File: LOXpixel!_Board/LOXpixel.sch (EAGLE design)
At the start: 18 parts, among them IC2 7805T, Q1 BSS138, Q2 BSS138

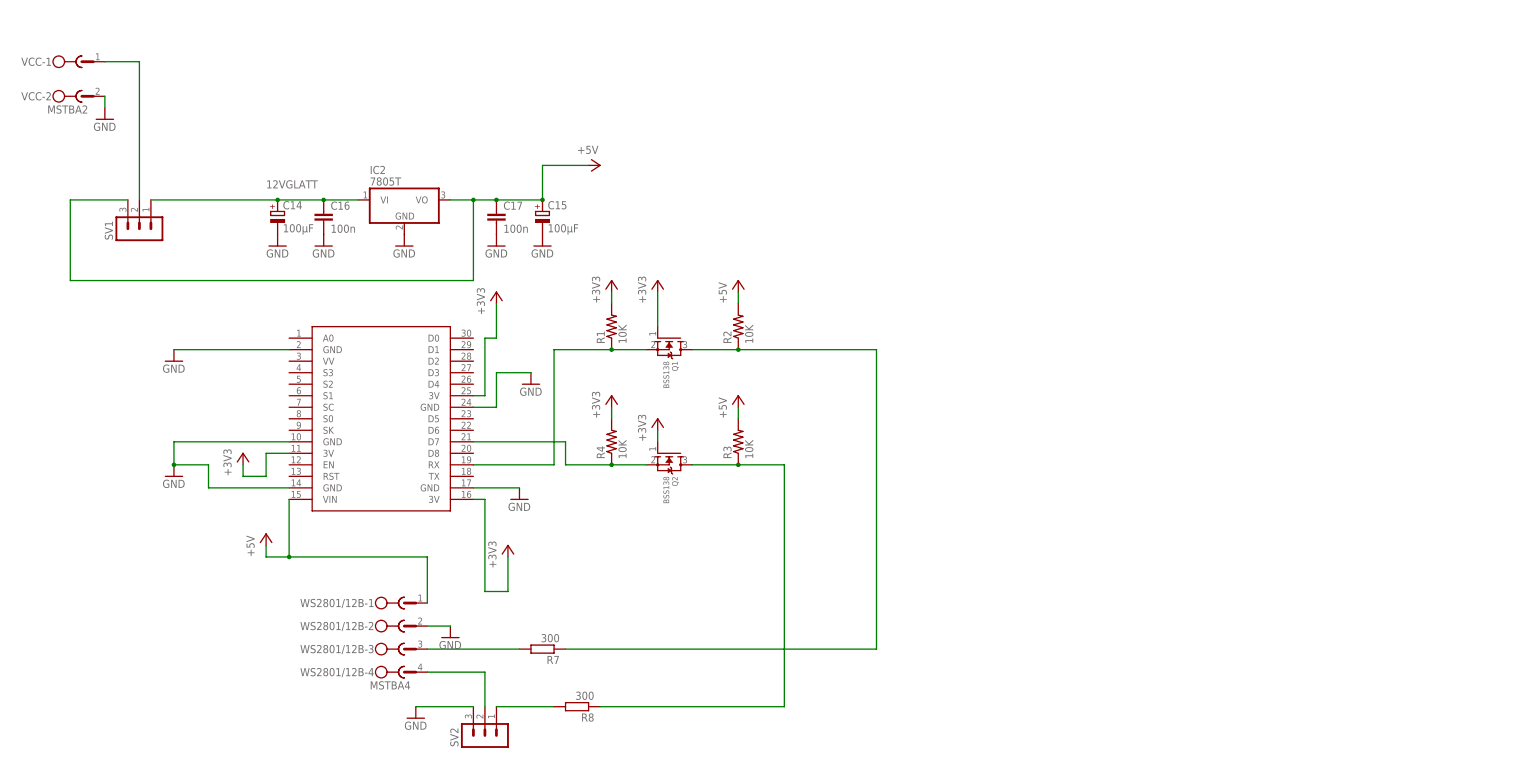
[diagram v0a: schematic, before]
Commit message: pcb for hammond 1551usb3 and rebuild without nodemcu and for esp-wroom-02
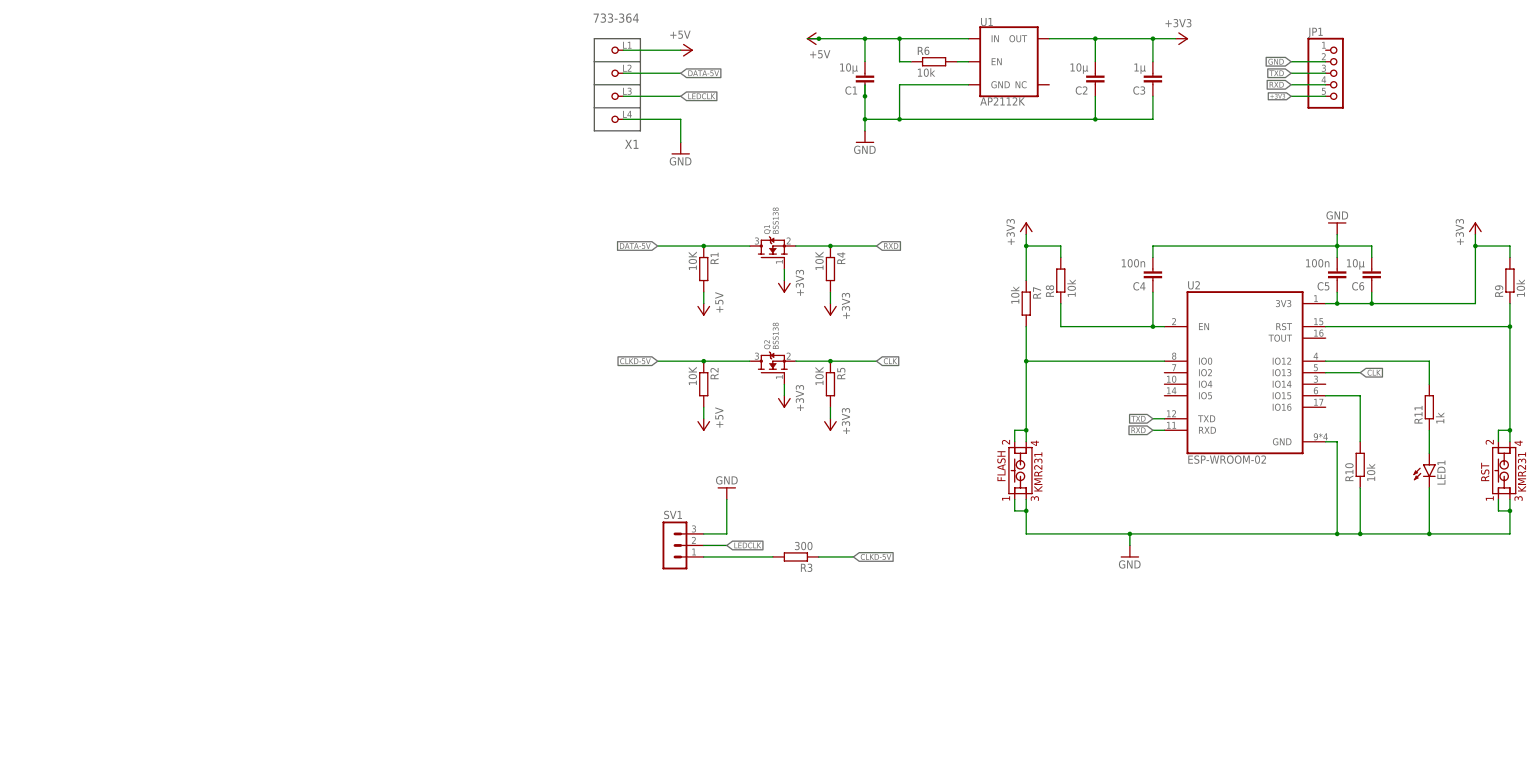
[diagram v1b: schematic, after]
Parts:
- removed C14, C15: 100µF, rcl:CPOL-EU150CLZ-0810
- removed C16, C17: 100n, rcl:C-EUC0805
- removed IC2: 7805T, linear:7805T
- removed SV2: (no value), con-lstb:MA03-1
- removed U$1: NODEMCU, nodemcu:NODEMCU
- removed VCC: MSTBA2, con-phoenix-508:MSTBA2
- removed WS2801/12B: MSTBA4, con-phoenix-508:MSTBA4
- added C1, C2, C6: 10µ, rcl:C-EUC0805
- added C3: 1µ, rcl:C-EUC0805
- added C4, C5: 100n, rcl:C-EUC0805
- added FLASH, RST: KMR231, eagle-book:KMR231
- added JP1: (no value), pinhead:PINHD-1X5
- added LED1: (no value), led:LEDCHIPLED_0805
- added R10, R6, R9: 10k, rcl:R-EU_R0805
- added R11: 1k, rcl:R-EU_R0805
- added R5: 10K, rcl:R-EU_R0805
- added U1: AP2112K, SparkFun-IC-Power:V_REG_AP2112K-3.3V
- added U2: ESP-WROOM-02, ESP-WROOM-02:ESP-WROOM-02
- added X1: 733-364, con-wago_2.5mm:733-364
- R1, R2, R4: device adafruit:R-US_R0805 -> rcl:R-EU_R0805
- R3: value 10K -> 300; device adafruit:R-US_R0805 -> rcl:R-EU_R0805
- R7: value 300 -> 10k; device rcl:R-EU_R0805 -> rcl:R-EU_M0805
- R8: value 300 -> 10k
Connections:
- removed net 12VGLATT: C14.+, C16.1, IC2.VI, SV1.1
- removed net N$11: Q2.S, R4.1, U$1.D7
- removed net N$12: Q2.D, R3.1, R8.1
- removed net N$4: SV2.2, WS2801/12B-4.1
- removed net N$5: R8.2, SV2.1
- removed net N$6: R7.2, WS2801/12B-3.1
- removed net N$7: Q1.S, R1.1, U$1.RX
- removed net N$8: Q1.D, R2.1, R7.1
- new net BOOTMODE: R10.2, U2.IO15
- new net CHIPEN: C4.1, R8.1, U2.EN
- new net CLK: Q2.S, R5.1, U2.IO13
- new net CLKD-5V: Q2.D, R2.1, R3.1
- new net DATA-5V: Q1.D, R1.1, X1.P2
- new net FLASH: FLASH.2, FLASH.4, R7.2, U2.IO0
- new net LEDCLK: SV1.2, X1.P3
- new net N$1: R6.2, U1.EN
- new net N$10: R3.2, SV1.1
- new net RST: R9.1, RST.2, RST.4, U2.RST
- new net RXD: JP1.4, Q1.S, R4.1, U2.RXD
- new net STATLED: R11.2, U2.IO12
- new net TXD: JP1.3, U2.TXD
- net +3V3: now also C2.2, C3.2, C5.1, C6.1, JP1.5, R5.2, R7.1, R8.2, R9.2, U1.OUT, U2.3V3; no longer R1.2, U$1.3V, U$1.3V@1, U$1.3V@2
- net +5V: now also C1.2, R1.2, R6.1, U1.IN, X1.P1; no longer C15.+, C17.1, IC2.VO, R3.2, SV1.3, U$1.VIN, WS2801/12B-1.1
- net GND: now also C1.1, C2.1, C3.1, C4.2, C5.2, C6.2, FLASH.1, FLASH.3, JP1.2, LED1.C, R10.1, RST.1, RST.3, SV1.3, U1.GND, U2.GND, X1.P4; no longer C14.-, C15.-, C16.2, C17.2, IC2.GND, SV2.3, U$1.GND, U$1.GND@1, U$1.GND@2, U$1.GND@3, U$1.GND@4, VCC-2.1, WS2801/12B-2.1
- net N$2: now also LED1.A, R11.1; no longer SV1.2, VCC-1.1
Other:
- moved on the sheet: Q1, Q2, R7, R8, SV1

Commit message: finished first board revision
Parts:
- R7: device rcl:R-EU_M0805 -> rcl:R-EU_R0805
- renumbered LED1 to STATUS, RST to RESET
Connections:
- net CLKD-5V renamed CLK-5V
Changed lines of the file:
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@@
 </classes>
 <parts>
-<part name="X1" library="con-wago_2.5mm" deviceset="733-364" device=""/>
+<part name="X1" library="con-wago_2.5mm" deviceset="733-364" device="" override_package3d_urn="urn:adsk.eagle:package:14797526/2" override_package_urn="urn:adsk.eagle:footprint:14797527/1"/>
 <part name="C1" library="rcl" library_urn="urn:adsk.eagle:library:334" deviceset="C-EU" device="C0805" package3d_urn="urn:adsk.eagle:package:23617/2" value="10µ"/>
 <part name="C2" library="rcl" library_urn="urn:adsk.eagle:library:334" deviceset="C-EU" device="C0805" package3d_urn="urn:adsk.eagle:package:23617/2" value="10µ"/>
@@
 <part name="R9" library="rcl" library_urn="urn:adsk.eagle:library:334" deviceset="R-EU_" device="R0805" package3d_urn="urn:adsk.eagle:package:23553/2" value="10k"/>
 <part name="+3V35" library="supply1" deviceset="+3V3" device=""/>
-<part name="R7" library="rcl" library_urn="urn:adsk.eagle:library:334" deviceset="R-EU_" device="M0805" package3d_urn="urn:adsk.eagle:package:23556/2" value="10k"/>
+<part name="R7" library="rcl" library_urn="urn:adsk.eagle:library:334" deviceset="R-EU_" device="R0805" package3d_urn="urn:adsk.eagle:package:23553/2" value="10k"/>
 <part name="+3V37" library="supply1" deviceset="+3V3" device=""/>
 <part name="GND5" library="supply1" deviceset="GND" device=""/>
@@
 <part name="R8" library="rcl" library_urn="urn:adsk.eagle:library:334" deviceset="R-EU_" device="R0805" package3d_urn="urn:adsk.eagle:package:23553/2" value="10k"/>
 <part name="C4" library="rcl" library_urn="urn:adsk.eagle:library:334" deviceset="C-EU" device="C0805" package3d_urn="urn:adsk.eagle:package:23617/2" value="100n"/>
-<part name="U2" library="ESP-WROOM-02" deviceset="ESP-WROOM-02" device="" override_package3d_urn="urn:adsk.eagle:package:13247454/2" override_package_urn="urn:adsk.eagle:footprint:13247455/1" override_locally_modified="yes"/>
+<part name="U2" library="ESP-WROOM-02" deviceset="ESP-WROOM-02" device="" override_package3d_urn="urn:adsk.eagle:package:14797501/2" override_package_urn="urn:adsk.eagle:footprint:14797502/1"/>
 <part name="R11" library="rcl" library_urn="urn:adsk.eagle:library:334" deviceset="R-EU_" device="R0805" package3d_urn="urn:adsk.eagle:package:23553/2" value="1k"/>
-<part name="LED1" library="led" library_urn="urn:adsk.eagle:library:259" deviceset="LED" device="CHIPLED_0805" package3d_urn="urn:adsk.eagle:package:15821/2"/>
+<part name="STATUS" library="led" library_urn="urn:adsk.eagle:library:259" deviceset="LED" device="CHIPLED_0805" package3d_urn="urn:adsk.eagle:package:15821/2"/>
 <part name="JP1" library="pinhead" library_urn="urn:adsk.eagle:library:325" deviceset="PINHD-1X5" device="" package3d_urn="urn:adsk.eagle:package:22469/2"/>
 <part name="P+1" library="supply1" deviceset="+5V" device=""/>
 <part name="GND1" library="supply1" deviceset="GND" device=""/>
-<part name="Q1" library="adafruit" deviceset="MOSFET-N" device="REFLOW" value="BSS138"/>
+<part name="Q1" library="adafruit" deviceset="MOSFET-N" device="REFLOW" override_package3d_urn="urn:adsk.eagle:package:14797484/2" override_package_urn="urn:adsk.eagle:footprint:14797485/1" value="BSS138"/>
 <part name="+3V31" library="supply1" deviceset="+3V3" device=""/>
 <part name="R1" library="rcl" library_urn="urn:adsk.eagle:library:334" deviceset="R-EU_" device="R0805" package3d_urn="urn:adsk.eagle:package:23553/2" value="10K"/>
@@
 <part name="P+2" library="supply1" deviceset="+5V" device=""/>
 <part name="R3" library="rcl" library_urn="urn:adsk.eagle:library:334" deviceset="R-EU_" device="R0805" package3d_urn="urn:adsk.eagle:package:23553/2" value="300"/>
-<part name="SV1" library="con-lstb" library_urn="urn:adsk.eagle:library:162" deviceset="MA03-1" device="" package3d_urn="urn:adsk.eagle:package:8339/1"/>
+<part name="SV1" library="con-lstb" library_urn="urn:adsk.eagle:library:162" deviceset="MA03-1" device="" package3d_urn="urn:adsk.eagle:package:8339/1" override_package3d_urn="urn:adsk.eagle:package:14797494/2" override_package_urn="urn:adsk.eagle:footprint:8281/1"/>
 <part name="GND2" library="supply1" deviceset="GND" device=""/>
-<part name="Q2" library="adafruit" deviceset="MOSFET-N" device="REFLOW" value="BSS138"/>
+<part name="Q2" library="adafruit" deviceset="MOSFET-N" device="REFLOW" override_package3d_urn="urn:adsk.eagle:package:14797490/2" override_package_urn="urn:adsk.eagle:footprint:14797491/1" value="BSS138"/>
 <part name="+3V32" library="supply1" deviceset="+3V3" device=""/>
 <part name="R2" library="rcl" library_urn="urn:adsk.eagle:library:334" deviceset="R-EU_" device="R0805" package3d_urn="urn:adsk.eagle:package:23553/2" value="10K"/>
@@
 <part name="FRAME1" library="frames" library_urn="urn:adsk.eagle:library:229" deviceset="A4L-LOC" device=""/>
 <part name="FLASH" library="eagle-book" deviceset="KMR231" device="" override_package3d_urn="urn:adsk.eagle:package:13489703/2" override_package_urn="urn:adsk.eagle:footprint:13489704/1"/>
-<part name="RST" library="eagle-book" deviceset="KMR231" device="" override_package3d_urn="urn:adsk.eagle:package:13489703/2" override_package_urn="urn:adsk.eagle:footprint:13489704/1"/>
+<part name="RESET" library="eagle-book" deviceset="KMR231" device="" override_package3d_urn="urn:adsk.eagle:package:13489703/2" override_package_urn="urn:adsk.eagle:footprint:13489704/1"/>
 </parts>
 <sheets>
@@
 <attribute name="VALUE" x="221.742" y="67.31" size="1.778" layer="96" rot="R90"/>
 </instance>
-<instance part="LED1" gate="G$1" x="218.44" y="58.42" smashed="yes">
+<instance part="STATUS" gate="G$1" x="218.44" y="58.42" smashed="yes">
 <attribute name="NAME" x="221.996" y="53.848" size="1.778" layer="95" rot="R90"/>
 <attribute name="VALUE" x="224.155" y="53.848" size="1.778" layer="96" rot="R90"/>
@@
 <attribute name="VALUE" x="133.096" y="52.324" size="1.778" layer="94" rot="R90"/>
 </instance>
-<instance part="RST" gate="G$1" x="233.68" y="58.42" smashed="yes" rot="R90">
+<instance part="RESET" gate="G$1" x="233.68" y="58.42" smashed="yes" rot="R90">
 <attribute name="NAME" x="231.648" y="54.61" size="1.778" layer="94" rot="R90"/>
 <attribute name="VALUE" x="239.776" y="52.324" size="1.778" layer="94" rot="R90"/>
@@
 <pinref part="R10" gate="G$1" pin="1"/>
 <pinref part="U2" gate="G$1" pin="GND"/>
-<pinref part="LED1" gate="G$1" pin="C"/>
+<pinref part="STATUS" gate="G$1" pin="C"/>
 <wire x1="129.54" y1="43.18" x2="129.54" y2="48.26" width="0.1524" layer="91"/>
 <wire x1="129.54" y1="43.18" x2="152.4" y2="43.18" width="0.1524" layer="91"/>
@@
 <wire x1="218.44" y1="43.18" x2="236.22" y2="43.18" width="0.1524" layer="91"/>
 <junction x="218.44" y="43.18"/>
-<pinref part="RST" gate="G$1" pin="3"/>
+<pinref part="RESET" gate="G$1" pin="3"/>
 <wire x1="236.22" y1="43.18" x2="236.22" y2="48.26" width="0.1524" layer="91"/>
-<pinref part="RST" gate="G$1" pin="1"/>
+<pinref part="RESET" gate="G$1" pin="1"/>
 <wire x1="236.22" y1="48.26" x2="236.22" y2="50.8" width="0.1524" layer="91"/>
 <wire x1="233.68" y1="50.8" x2="233.68" y2="48.26" width="0.1524" layer="91"/>
@@
 <pinref part="R9" gate="G$1" pin="1"/>
 <pinref part="U2" gate="G$1" pin="RST"/>
-<pinref part="RST" gate="G$1" pin="4"/>
-<pinref part="RST" gate="G$1" pin="2"/>
+<pinref part="RESET" gate="G$1" pin="4"/>
+<pinref part="RESET" gate="G$1" pin="2"/>
 <wire x1="236.22" y1="66.04" x2="236.22" y2="88.9" width="0.1524" layer="91"/>
 <wire x1="233.68" y1="63.5" x2="233.68" y2="66.04" width="0.1524" layer="91"/>
@@
 <wire x1="218.44" y1="66.04" x2="218.44" y2="60.96" width="0.1524" layer="91"/>
 <pinref part="R11" gate="G$1" pin="1"/>
-<pinref part="LED1" gate="G$1" pin="A"/>
+<pinref part="STATUS" gate="G$1" pin="A"/>
 </segment>
 </net>
@@
 </segment>
 </net>
-<net name="CLKD-5V" class="0">
+<net name="CLK-5V" class="0">
 <segment>
 <pinref part="R3" gate="G$1" pin="1"/>
